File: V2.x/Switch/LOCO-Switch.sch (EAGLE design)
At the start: 55 parts, among them IC1 Atmega 328-P, IC2 MCP2515, IC3 ACS712ELCTR-20A-T, IC5 LM340MP-05, J1 3-794618-4, J2 3-794618-4, Q1 8MHz, Q2 16MHz, Q3 FDS5680, Q4 FDS5680, Q5 FDS5680, Q6 FDS5680, Q7 FDS5680, Q8 FDS5680, X1 22-23-2081

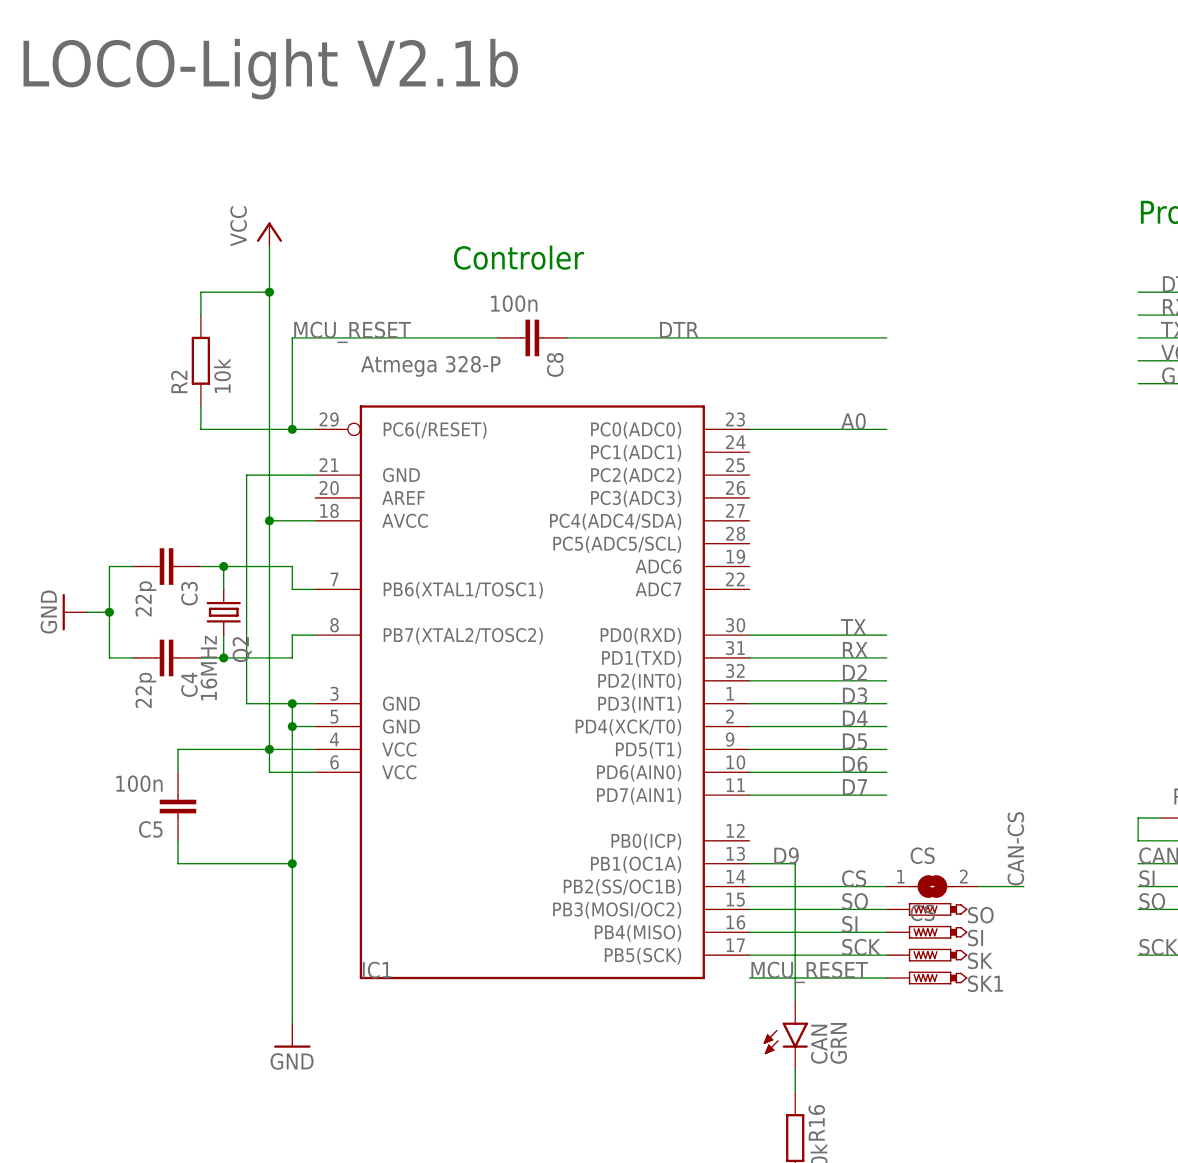
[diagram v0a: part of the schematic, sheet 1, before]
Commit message: added Loco-CAN icon to motor, servo and switch boards
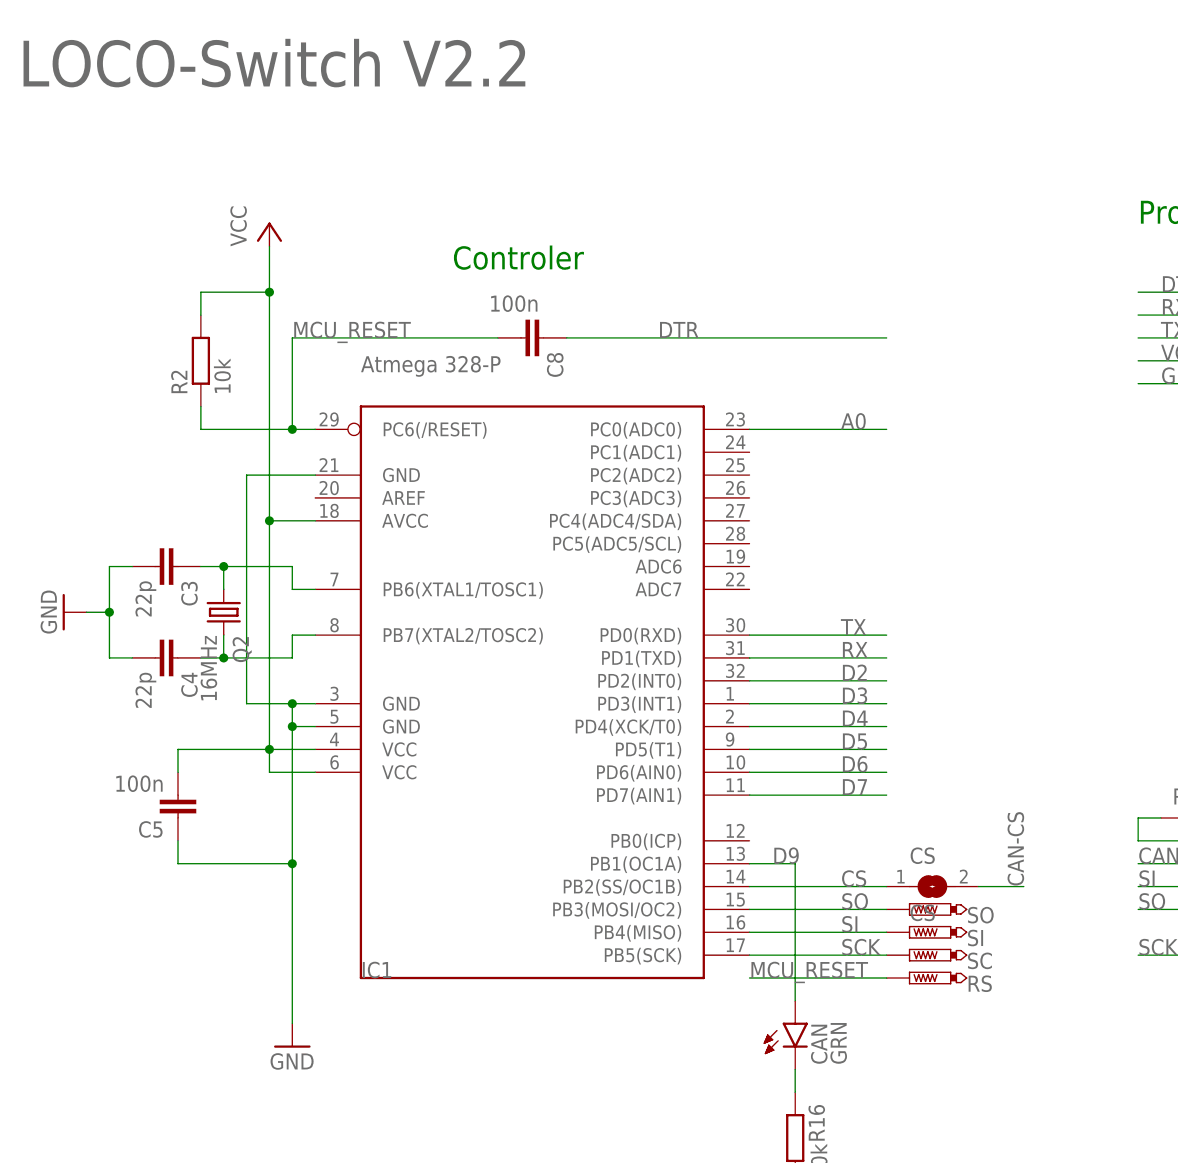
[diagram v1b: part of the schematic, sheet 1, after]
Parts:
- renumbered SK to SC, SK1 to RS
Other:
- note added: "LOCO-Switch V2.2"
- note removed: "LOCO-Light V2.1b"
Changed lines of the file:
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@@
 <part name="P+4" library="supply1" library_urn="urn:adsk.eagle:library:371" deviceset="+12V" device=""/>
 <part name="X1" library="con-molex" library_urn="urn:adsk.eagle:library:165" deviceset="22-23-2081" device="" package3d_urn="urn:adsk.eagle:package:8078639/1"/>
-<part name="SO" library="testpad" library_urn="urn:adsk.eagle:library:385" deviceset="PTR1" device="B1,27" package3d_urn="urn:adsk.eagle:package:27944/1"/>
-<part name="SI" library="testpad" library_urn="urn:adsk.eagle:library:385" deviceset="PTR1" device="B1,27" package3d_urn="urn:adsk.eagle:package:27944/1"/>
-<part name="SK" library="testpad" library_urn="urn:adsk.eagle:library:385" deviceset="PTR1" device="B1,27" package3d_urn="urn:adsk.eagle:package:27944/1"/>
+<part name="SO" library="testpad" library_urn="urn:adsk.eagle:library:385" deviceset="PTR1" device="B1,27" package3d_urn="urn:adsk.eagle:package:27944/2"/>
+<part name="SI" library="testpad" library_urn="urn:adsk.eagle:library:385" deviceset="PTR1" device="B1,27" package3d_urn="urn:adsk.eagle:package:27944/2"/>
+<part name="SC" library="testpad" library_urn="urn:adsk.eagle:library:385" deviceset="PTR1" device="B1,27" package3d_urn="urn:adsk.eagle:package:27944/2"/>
 <part name="CS" library="jumper" library_urn="urn:adsk.eagle:library:252" deviceset="SJ" device="" package3d_urn="urn:adsk.eagle:package:15471/1" value="CS"/>
 <part name="CAN" library="led" library_urn="urn:adsk.eagle:library:259" deviceset="LED" device="CHIP-LED0603" package3d_urn="urn:adsk.eagle:package:15819/3" value="GRN"/>
 <part name="R16" library="rcl" library_urn="urn:adsk.eagle:library:334" deviceset="R-EU_" device="R0603" package3d_urn="urn:adsk.eagle:package:23555/3" value="10k"/>
 <part name="GND10" library="supply1" library_urn="urn:adsk.eagle:library:371" deviceset="GND" device=""/>
-<part name="SK1" library="testpad" library_urn="urn:adsk.eagle:library:385" deviceset="PTR1" device="B1,27" package3d_urn="urn:adsk.eagle:package:27944/1"/>
+<part name="RS" library="testpad" library_urn="urn:adsk.eagle:library:385" deviceset="PTR1" device="B1,27" package3d_urn="urn:adsk.eagle:package:27944/2"/>
 </parts>
 <sheets>
@@
 <text x="114.3" y="45.72" size="2.54" layer="91" grouprefs="CAN-INTERFACE">CAN-Interface</text>
 <text x="22.86" y="93.98" size="2.54" layer="91" grouprefs="MCU">Controler</text>
-<text x="-25.4" y="114.3" size="5.08" layer="95">LOCO-Light V2.1b</text>
+<text x="-25.4" y="114.3" size="5.08" layer="95">LOCO-Switch V2.2</text>
 </plain>
 <instances>
@@
 <attribute name="TP_SIGNAL_NAME" x="76.2" y="21.59" size="1.778" layer="97" rot="R90"/>
 </instance>
-<instance part="SK" gate="G$1" x="73.66" y="17.78" smashed="yes" rot="R90" grouprefs="MCU">
+<instance part="SC" gate="G$1" x="73.66" y="17.78" smashed="yes" rot="R90" grouprefs="MCU">
 <attribute name="NAME" x="80.01" y="16.256" size="1.778" layer="95"/>
 <attribute name="TP_SIGNAL_NAME" x="76.2" y="19.05" size="1.778" layer="97" rot="R90"/>
@@
 <attribute name="VALUE" x="58.42" y="-15.24" size="1.778" layer="96"/>
 </instance>
-<instance part="SK1" gate="G$1" x="73.66" y="15.24" smashed="yes" rot="R90" grouprefs="MCU">
+<instance part="RS" gate="G$1" x="73.66" y="15.24" smashed="yes" rot="R90" grouprefs="MCU">
 <attribute name="NAME" x="80.01" y="13.716" size="1.778" layer="95"/>
 <attribute name="TP_SIGNAL_NAME" x="76.2" y="16.51" size="1.778" layer="97" rot="R90"/>
@@
 <wire x1="7.62" y1="-53.34" x2="22.86" y2="-53.34" width="0.1524" layer="91" grouprefs="POWER"/>
 <wire x1="22.86" y1="-53.34" x2="22.86" y2="-48.26" width="0.1524" layer="91" grouprefs="POWER"/>
-<pinref part="C13" gate="G$1" pin="-"/>
 <wire x1="0" y1="-50.8" x2="0" y2="-53.34" width="0.1524" layer="91" grouprefs="POWER"/>
 <junction x="0" y="-53.34" grouprefs="POWER"/>
@@
 <wire x1="35.56" y1="-53.34" x2="35.56" y2="-50.8" width="0.1524" layer="91" grouprefs="POWER"/>
 <junction x="22.86" y="-53.34" grouprefs="POWER"/>
-<pinref part="C16" gate="G$1" pin="-"/>
 <wire x1="35.56" y1="-53.34" x2="43.18" y2="-53.34" width="0.1524" layer="91" grouprefs="POWER"/>
 <wire x1="43.18" y1="-53.34" x2="43.18" y2="-50.8" width="0.1524" layer="91" grouprefs="POWER"/>
@@
 <wire x1="71.12" y1="-58.42" x2="73.66" y2="-58.42" width="0.1524" layer="91" grouprefs="POWER"/>
 <junction x="73.66" y="-58.42" grouprefs="POWER"/>
+<pinref part="C13" gate="G$1" pin="-"/>
+<pinref part="C16" gate="G$1" pin="-"/>
 <pinref part="IC5" gate="A" pin="GND"/>
 </segment>
@@
 <wire x1="35.56" y1="-43.18" x2="35.56" y2="-40.64" width="0.1524" layer="91" grouprefs="POWER"/>
 <junction x="35.56" y="-40.64" grouprefs="POWER"/>
-<pinref part="C16" gate="G$1" pin="+"/>
 <wire x1="43.18" y1="-43.18" x2="43.18" y2="-40.64" width="0.1524" layer="91" grouprefs="POWER"/>
 <junction x="43.18" y="-40.64" grouprefs="POWER"/>
@@
 <wire x1="50.8" y1="-43.18" x2="50.8" y2="-40.64" width="0.1524" layer="91" grouprefs="POWER"/>
 <junction x="50.8" y="-40.64" grouprefs="POWER"/>
-<pinref part="+5V" gate="G$1" pin="A"/>
 <wire x1="58.42" y1="-40.64" x2="58.42" y2="-43.18" width="0.1524" layer="91" grouprefs="POWER"/>
 <junction x="58.42" y="-40.64" grouprefs="POWER"/>
+<pinref part="C16" gate="G$1" pin="+"/>
+<pinref part="+5V" gate="G$1" pin="A"/>
 <pinref part="IC5" gate="A" pin="VO"/>
 </segment>
@@
 <pinref part="IC1" gate="G$1" pin="PB5(SCK)"/>
 <label x="66.04" y="17.78" size="1.778" layer="95" grouprefs="MCU"/>
-<pinref part="SK" gate="G$1" pin="TP"/>
+<pinref part="SC" gate="G$1" pin="TP"/>
 </segment>
 <segment>
@@
 </segment>
 <segment>
-<pinref part="SK1" gate="G$1" pin="TP"/>
 <wire x1="71.12" y1="15.24" x2="55.88" y2="15.24" width="0.1524" layer="91" grouprefs="MCU"/>
 <label x="55.88" y="15.24" size="1.778" layer="95" grouprefs="MCU"/>
+<pinref part="RS" gate="G$1" pin="TP"/>
 </segment>
 </net>
@@
 <wire x1="-7.62" y1="-43.18" x2="-7.62" y2="-40.64" width="0.1524" layer="91" grouprefs="POWER"/>
 <junction x="-7.62" y="-40.64" grouprefs="POWER"/>
-<pinref part="C13" gate="G$1" pin="+"/>
 <wire x1="0" y1="-43.18" x2="0" y2="-40.64" width="0.1524" layer="91" grouprefs="POWER"/>
 <junction x="0" y="-40.64" grouprefs="POWER"/>
@@
 <wire x1="7.62" y1="-43.18" x2="7.62" y2="-40.64" width="0.1524" layer="91" grouprefs="POWER"/>
 <junction x="7.62" y="-40.64" grouprefs="POWER"/>
+<pinref part="C13" gate="G$1" pin="+"/>
 <pinref part="IC5" gate="A" pin="VI"/>
 </segment>
@@
 <net name="N$12" class="0">
 <segment>
-<pinref part="+5V" gate="G$1" pin="C"/>
 <pinref part="R15" gate="G$1" pin="2"/>
 <wire x1="58.42" y1="-50.8" x2="58.42" y2="-58.42" width="0.1524" layer="91" grouprefs="POWER"/>
 <wire x1="58.42" y1="-58.42" x2="60.96" y2="-58.42" width="0.1524" layer="91" grouprefs="POWER"/>
+<pinref part="+5V" gate="G$1" pin="C"/>
 </segment>
 </net>
@@
 </segment>
 <segment>
-<pinref part="CS" gate="1" pin="2"/>
 <wire x1="81.28" y1="25.4" x2="86.36" y2="25.4" width="0.1524" layer="91" grouprefs="MCU"/>
 <label x="86.36" y="25.4" size="1.778" layer="95" rot="R90" grouprefs="MCU"/>
+<pinref part="CS" gate="1" pin="2"/>
 </segment>
 </net>
@@
 <segment>
 <pinref part="R16" gate="G$1" pin="1"/>
+<wire x1="60.96" y1="2.54" x2="60.96" y2="5.08" width="0.1524" layer="91" grouprefs="MCU"/>
 <pinref part="CAN" gate="G$1" pin="C"/>
-<wire x1="60.96" y1="2.54" x2="60.96" y2="5.08" width="0.1524" layer="91" grouprefs="MCU"/>
 </segment>
 </net>
 <net name="D9" class="0">
 <segment>
-<pinref part="CAN" gate="G$1" pin="A"/>
 <pinref part="IC1" gate="G$1" pin="PB1(OC1A)"/>
 <wire x1="60.96" y1="12.7" x2="60.96" y2="27.94" width="0.1524" layer="91" grouprefs="MCU"/>
 <wire x1="60.96" y1="27.94" x2="55.88" y2="27.94" width="0.1524" layer="91" grouprefs="MCU"/>
 <label x="58.42" y="27.94" size="1.778" layer="95" grouprefs="MCU"/>
-</segment>
-</net>
+<pinref part="CAN" gate="G$1" pin="A"/>
+</segment>
+</net>

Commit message: design clean up
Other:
- note added: "Loco-Switch V2.2"
- note removed: "LOCO-Switch V2.2"
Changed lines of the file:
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@@
 <text x="114.3" y="45.72" size="2.54" layer="91" grouprefs="CAN-INTERFACE">CAN-Interface</text>
 <text x="22.86" y="93.98" size="2.54" layer="91" grouprefs="MCU">Controler</text>
-<text x="-25.4" y="114.3" size="5.08" layer="95">LOCO-Switch V2.2</text>
+<text x="-25.4" y="114.3" size="5.08" layer="95">Loco-Switch V2.2</text>
 </plain>
 <instances>
